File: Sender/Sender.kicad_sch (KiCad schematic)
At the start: 8 parts, among them SW1 SW_MEC_5G, U1 NUCLEO64-F401RE, U2 HM-10

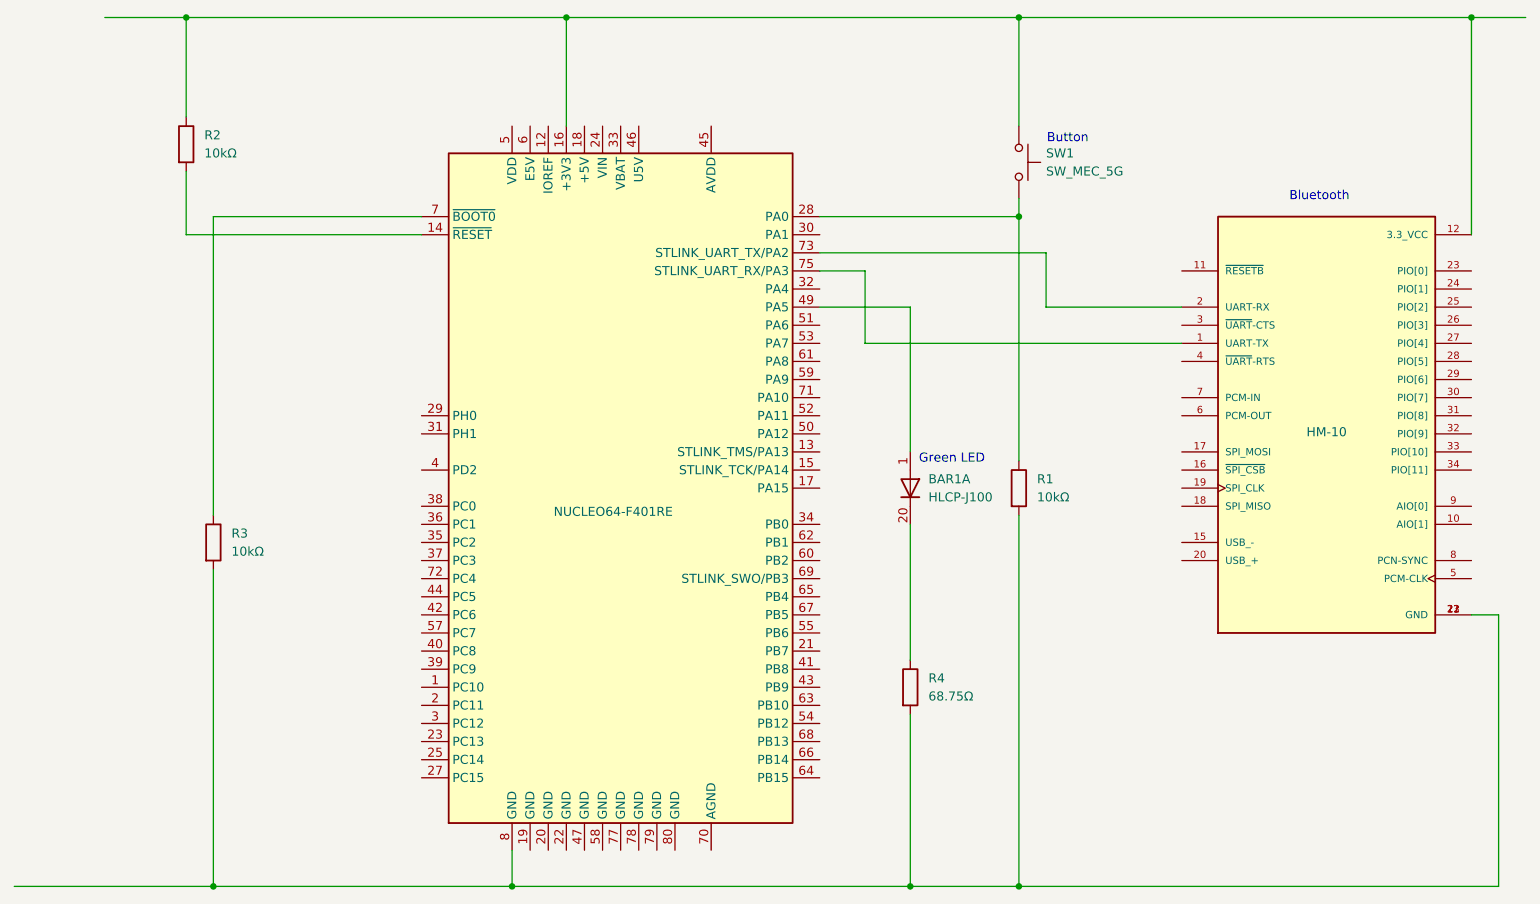
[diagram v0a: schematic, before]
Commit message: Rematch pins and Reset the resistor of green led
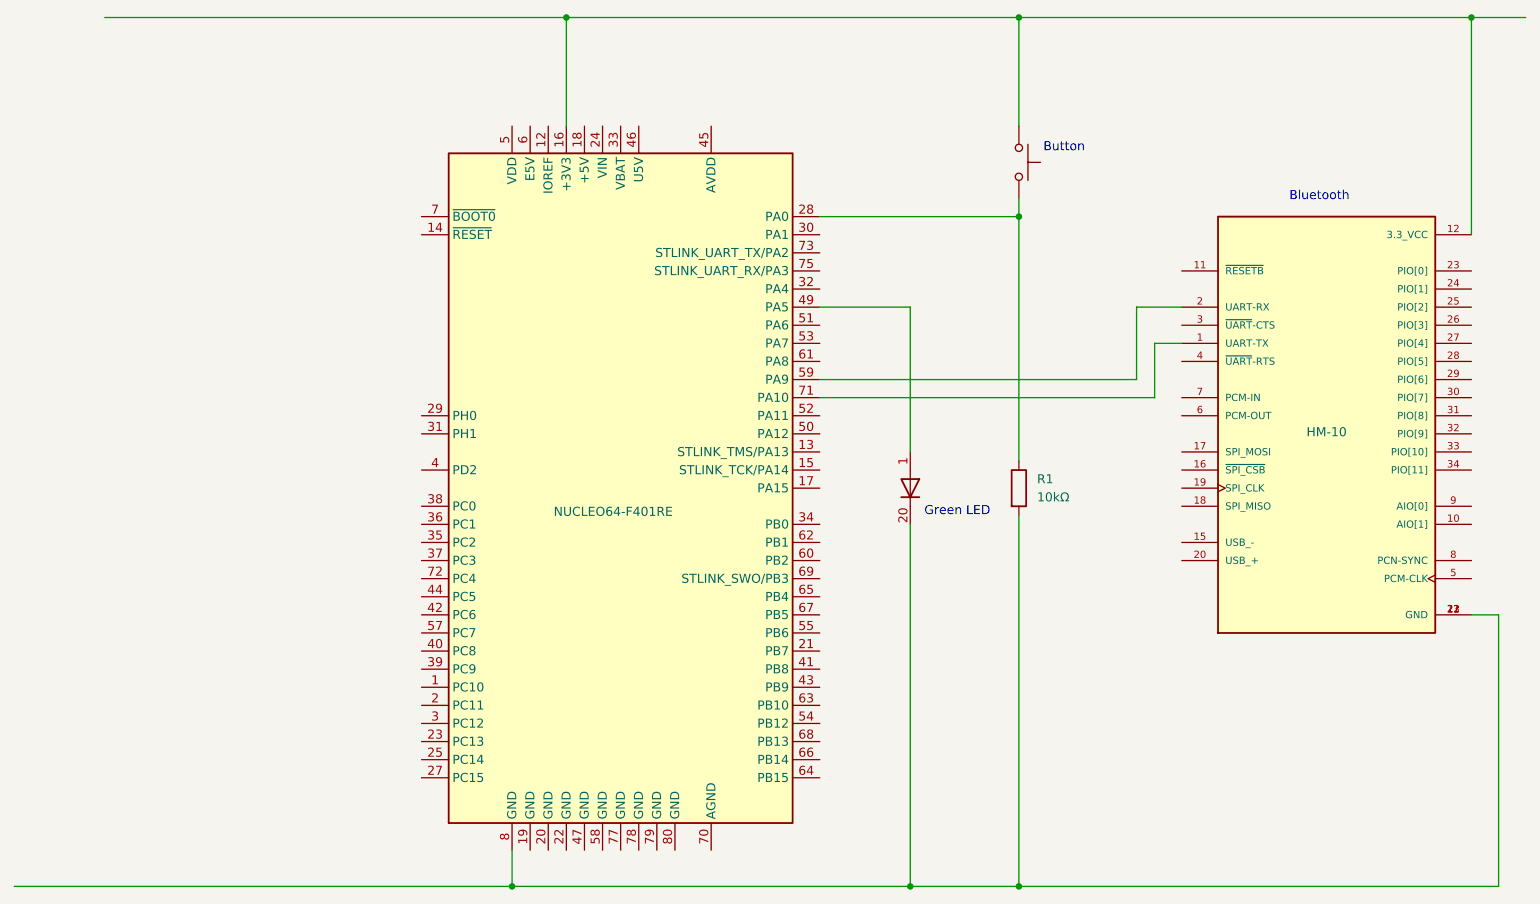
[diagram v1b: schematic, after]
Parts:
- removed R2, R3: 10kΩ, symbol Device:R
- removed R4: 68.75Ω, symbol Device:R
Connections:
- net at U2.1 (UART-TX): now also U1.71 (PA10); no longer U1.75 (STLINK_UART_RX/PA3)
- net at R1.2, U1.8 (GND), U2.13 (GND)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: now also BAR1.20 (K)
- net at U2.2 (UART-RX): now also U1.59 (PA9); no longer U1.73 (STLINK_UART_TX/PA2)

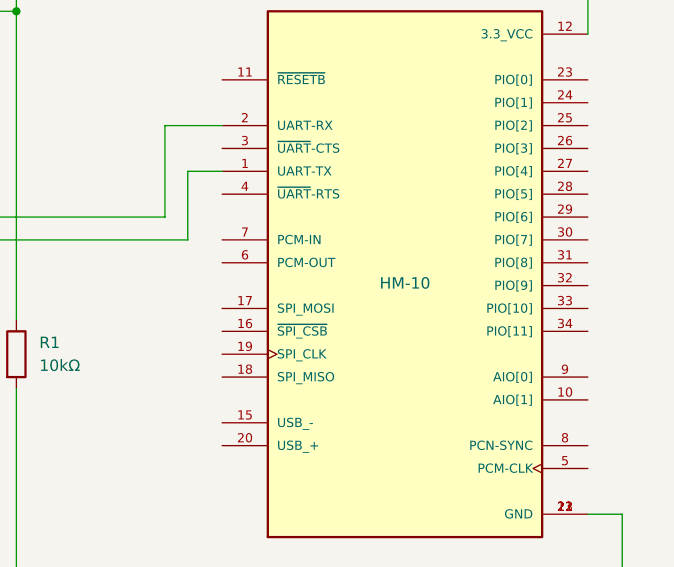
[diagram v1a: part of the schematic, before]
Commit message: Update the Bluetooth module to be HC-05
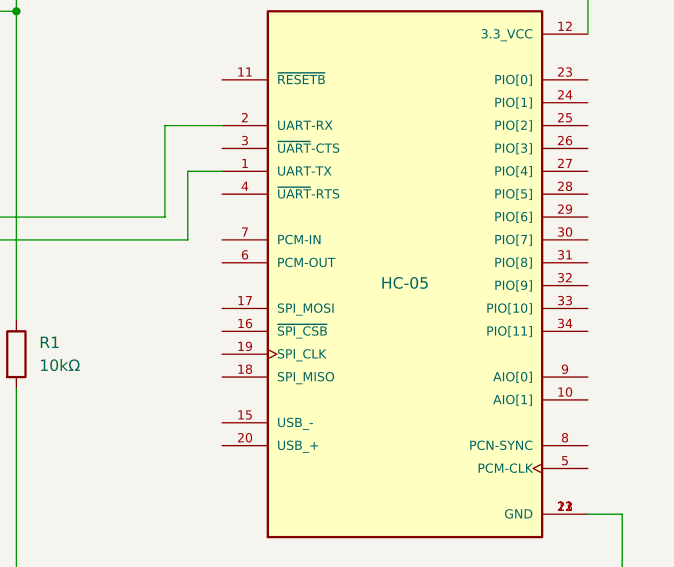
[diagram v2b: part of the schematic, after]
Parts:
- U2: value HM-10 -> HC-05
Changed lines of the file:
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@@
 			)
 		)
-		(property "Value" "HM-10"
+		(property "Value" "HC-05"
 			(at 213.36 88.646 0)
 			(effects

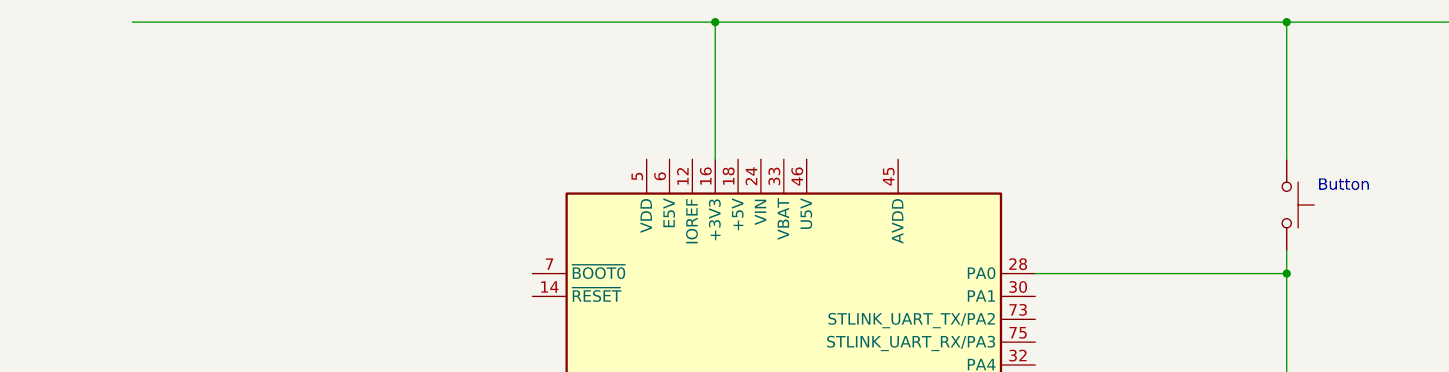
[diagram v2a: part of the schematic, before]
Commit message: Update Voltage supply to be 5 volts
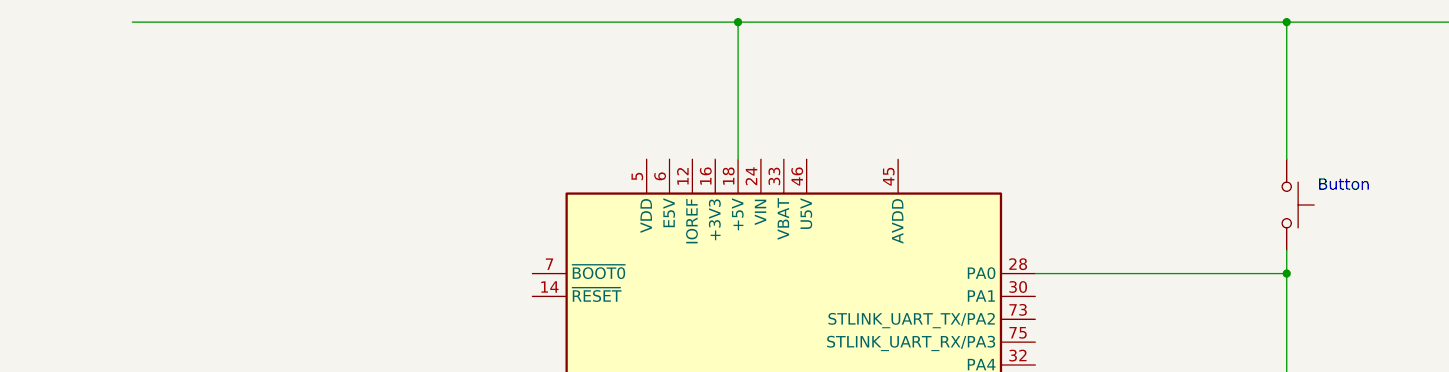
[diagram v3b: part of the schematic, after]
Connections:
- net at SW1.1 (A), SW1.2 (A), U2.12 (3.3_VCC): now also U1.18 (+5V); no longer U1.16 (+3V3)
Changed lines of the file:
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@@
-	)
-	(junction
-		(at 106.68 30.48)
-		(diameter 0)
-		(color 0 0 0 0)
 	)
 	(junction
@@
 		(color 0 0 0 0)
 	)
+	(junction
+		(at 109.22 30.48)
+		(diameter 0)
+		(color 0 0 0 0)
+	)
 	(wire
 		(pts
@@
 	(wire
 		(pts
+			(xy 109.22 30.48) (xy 170.18 30.48)
+		)
+		(stroke
+			(width 0)
+			(type default)
+			(color 255 0 0 1)
+		)
+	)
+	(wire
+		(pts
 			(xy 142.24 83.82) (xy 189.23 83.82)
 		)
@@
 	(wire
 		(pts
-			(xy 106.68 30.48) (xy 170.18 30.48)
+			(xy 41.91 30.48) (xy 109.22 30.48)
 		)
 		(stroke
@@
 	(wire
 		(pts
-			(xy 41.91 30.48) (xy 106.68 30.48)
-		)
-		(stroke
-			(width 0)
-			(type default)
-			(color 255 0 0 1)
-		)
-	)
-	(wire
-		(pts
-			(xy 106.68 30.48) (xy 106.68 45.72)
-		)
-		(stroke
-			(width 0)
-			(type default)
-			(color 255 0 0 1)
-		)
-	)
-	(wire
-		(pts
 			(xy 233.68 30.48) (xy 241.3 30.48)
 		)
 		(stroke
+			(width 0)
+			(type default)
+			(color 255 0 0 1)
+		)
+	)
+	(wire
+		(pts
+			(xy 109.22 30.48) (xy 109.22 45.72)
+		)
+		(stroke
